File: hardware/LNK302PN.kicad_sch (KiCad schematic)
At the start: 7 parts, among them J101 AC, J102 PWM, J103 380OUT, J104 380_BP2876D, J105 LOAD, J107 3V3, J108 380_LNK302PN

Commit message: LNK302PN
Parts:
- removed J101: AC, TerminalBlock_Phoenix:TerminalBlock_Phoenix_MKDS-1,5-2-5.08_1x02_P5.08mm_Horizontal, symbol Connector:Screw_Terminal_01x02
- removed J102: PWM, TerminalBlock_Phoenix:TerminalBlock_Phoenix_MKDS-1-2-3.81_1x02_P3.81mm_Horizontal, symbol Connector:Screw_Terminal_01x02
- removed J103: 380OUT, TerminalBlock_Phoenix:TerminalBlock_Phoenix_MKDS-1,5-2-5.08_1x02_P5.08mm_Horizontal, symbol Connector:Screw_Terminal_01x02
- removed J104: 380_BP2876D, TerminalBlock_Phoenix:TerminalBlock_Phoenix_MKDS-1,5-2-5.08_1x02_P5.08mm_Horizontal, symbol Connector:Screw_Terminal_01x02
- removed J105: LOAD, TerminalBlock_Phoenix:TerminalBlock_Phoenix_MKDS-1,5-2-5.08_1x02_P5.08mm_Horizontal, symbol Connector:Screw_Terminal_01x02
- removed J107: 3V3, TerminalBlock_Phoenix:TerminalBlock_Phoenix_MKDS-1,5-2-5.08_1x02_P5.08mm_Horizontal, symbol Connector:Screw_Terminal_01x02
- removed J108: 380_LNK302PN, TerminalBlock_Phoenix:TerminalBlock_Phoenix_MKDS-1,5-2-5.08_1x02_P5.08mm_Horizontal, symbol Connector:Screw_Terminal_01x02
- added C401, C404, C405: 100nF, Capacitor_THT:C_Disc_D5.0mm_W2.5mm_P5.00mm, symbol Device:C
- added C402: 10uF 16V, Capacitor_THT:CP_Radial_D5.0mm_P2.50mm, symbol Device:C_Polarized
- added C403: 470uF 10V, Capacitor_THT:CP_Radial_D10.0mm_P5.00mm, symbol Device:C_Polarized
- added C406: 100uF 10V, Capacitor_THT:CP_Radial_D6.3mm_P2.50mm, symbol Device:C_Polarized
- added D401: ES1J, Diode_THT:D_DO-41_SOD81_P7.62mm_Horizontal, symbol Device:D
- added D402: US1M, Diode_THT:D_DO-41_SOD81_P7.62mm_Horizontal, symbol Device:D
- added L401: 2.2mH, Inductor_THT:L_Radial_D10.0mm_P5.00mm_Fastron_07M, symbol Device:L
- added R401: 2.2K, Resistor_THT:R_Axial_DIN0207_L6.3mm_D2.5mm_P7.62mm_Horizontal, symbol Device:R
- added R402: 4.7K, Resistor_THT:R_Axial_DIN0207_L6.3mm_D2.5mm_P7.62mm_Horizontal, symbol Device:R
- added U401: AMS1117-3.3, Package_TO_SOT_SMD:SOT-223-3_TabPin2, symbol Regulator_Linear:AMS1117-3.3
- added U402: LNK306P, Package_DIP:PowerIntegrations_PDIP-8B, symbol Regulator_Switching:LNK306P
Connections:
- new net: C402.1, D402.1 (K), R402.1
- new net: C401.1, C402.2, D401.1 (K), L401.1, R401.1, U402.1 (S), U402.2 (S), U402.7 (S), U402.8 (S)
- new net: C401.2, U402.3 (BP)
- new net: R401.2, R402.2, U402.4 (FB)
- new net 380V: U402.5 (D)
- new net 3V3: C405.2, C406.1, U401.2 (VO)
- new net 5V: C403.1, C404.2, D402.2 (A), L401.2, U401.3 (VI)
- new net GND: C403.2, C404.1, C405.1, C406.2, D401.2 (A), U401.1 (GND)
- no-connect marks 1 -> 0
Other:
- removed sheet ACInput
- removed sheet BP2876D
- removed sheet BP2956XS
- removed sheet LNK302PN

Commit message: Prototype
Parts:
- renumbered C404 to C401, C401 to C402, C406 to C403, C402 to C404, C403 to C406, U402 to U401, U401 to U402
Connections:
- net 380V renamed 325V
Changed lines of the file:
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@@
 		)
 	)
-	(hierarchical_label "380V"
+	(hierarchical_label "325V"
 		(shape input)
 		(at 76.2 81.28 180)
@@
 		(dnp no)
 		(fields_autoplaced yes)
-		(property "Reference" "C402"
+		(property "Reference" "C404"
 			(at 179.07 72.7709 0)
 			(effects
@@
 			(project "NosLed"
 				(path "/473a9690-2801-417b-8084-b7ef486d51ca/28bc7e25-99ca-436a-bb17-be814d11a6d1"
-					(reference "C402")
+					(reference "C404")
 					(unit 1)
 				)
@@
 		(dnp no)
 		(fields_autoplaced yes)
-		(property "Reference" "C403"
+		(property "Reference" "C406"
 			(at 218.44 88.0109 0)
 			(effects
@@
 			(project "NosLed"
 				(path "/473a9690-2801-417b-8084-b7ef486d51ca/28bc7e25-99ca-436a-bb17-be814d11a6d1"
-					(reference "C403")
+					(reference "C406")
 					(unit 1)
 				)
@@
 		(dnp no)
 		(fields_autoplaced yes)
-		(property "Reference" "U402"
+		(property "Reference" "U401"
 			(at 109.22 88.9 0)
 			(effects
@@
 			(project ""
 				(path "/473a9690-2801-417b-8084-b7ef486d51ca/28bc7e25-99ca-436a-bb17-be814d11a6d1"
-					(reference "U402")
+					(reference "U401")
 					(unit 1)
 				)
@@
 		(dnp no)
 		(fields_autoplaced yes)
-		(property "Reference" "C404"
+		(property "Reference" "C401"
 			(at 123.19 125.7299 0)
 			(effects
@@
 			(project "NosLed"
 				(path "/473a9690-2801-417b-8084-b7ef486d51ca/28bc7e25-99ca-436a-bb17-be814d11a6d1"
-					(reference "C404")
+					(reference "C401")
 					(unit 1)
 				)
@@
 		(dnp no)
 		(fields_autoplaced yes)
-		(property "Reference" "C401"
+		(property "Reference" "C402"
 			(at 130.81 73.6599 0)
 			(effects
@@
 			(project "NosLed"
 				(path "/473a9690-2801-417b-8084-b7ef486d51ca/28bc7e25-99ca-436a-bb17-be814d11a6d1"
-					(reference "C401")
+					(reference "C402")
 					(unit 1)
 				)
@@
 		(dnp no)
 		(fields_autoplaced yes)
-		(property "Reference" "C406"
+		(property "Reference" "C403"
 			(at 158.75 124.8409 0)
 			(effects
@@
 			(project "NosLed"
 				(path "/473a9690-2801-417b-8084-b7ef486d51ca/28bc7e25-99ca-436a-bb17-be814d11a6d1"
-					(reference "C406")
+					(reference "C403")
 					(unit 1)
 				)
@@
 		(dnp no)
 		(fields_autoplaced yes)
-		(property "Reference" "U401"
+		(property "Reference" "U402"
 			(at 143.51 111.76 0)
 			(effects
@@
 			(project ""
 				(path "/473a9690-2801-417b-8084-b7ef486d51ca/28bc7e25-99ca-436a-bb17-be814d11a6d1"
-					(reference "U401")
-					(unit 1)
-				)
+					(reference "U402")
+					(unit 1)
+				)

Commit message: Tracing draft
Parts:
- removed C401, C405: 100nF, Capacitor_THT:C_Disc_D5.0mm_W2.5mm_P5.00mm, symbol Device:C
- removed C403: 100uF 10V, Capacitor_THT:CP_Radial_D6.3mm_P2.50mm, symbol Device:C_Polarized
- removed C404: 10uF 16V, Capacitor_THT:CP_Radial_D5.0mm_P2.50mm, symbol Device:C_Polarized
- removed D401: ES1J, Diode_THT:D_DO-41_SOD81_P7.62mm_Horizontal, symbol Device:D
- removed D402: US1M, Diode_THT:D_DO-41_SOD81_P7.62mm_Horizontal, symbol Device:D
- removed U401: LNK306P, Package_DIP:PowerIntegrations_PDIP-8B, symbol Regulator_Switching:LNK306P
- removed U402: AMS1117-3.3, Package_TO_SOT_SMD:SOT-223-3_TabPin2, symbol Regulator_Linear:AMS1117-3.3
- added C402: 10uF 16V, Capacitor_SMD:C_0805_2012Metric_Pad1.18x1.45mm_HandSolder, symbol Device:C
- added D401, D402: US1M, Diode_SMD:D_SMA, symbol Diode:US1M
- added U401: LNK306D, Package_SO:SOIC-8_3.9x4.9mm_P1.27mm, symbol Regulator_Switching:LNK306D
- C401: renamed from C402; footprint Capacitor_THT:C_Disc_D5.0mm_W2.5mm_P5.00mm -> Capacitor_SMD:C_0201_0603Metric_Pad0.64x0.40mm_HandSolder
- L401: footprint Inductor_THT:L_Radial_D10.0mm_P5.00mm_Fastron_07M -> Inductor_THT:L_Radial_D12.0mm_P5.00mm_Neosid_SD12k_style2
- R401, R402: footprint Resistor_THT:R_Axial_DIN0207_L6.3mm_D2.5mm_P7.62mm_Horizontal -> Resistor_SMD:R_0201_0603Metric_Pad0.64x0.40mm_HandSolder
- renumbered C406 to C403
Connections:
- net 325V: now also U401.4 (D)
- net 5V: now also D402.1 (K)
- net GND: now also D401.2 (A)
- net at R402.1: now also C402.2, D402.2 (A)
- net at C401.1, L401.1, R401.1: now also C402.1, D401.1 (K), U401.5 (S), U401.6 (S), U401.7 (S), U401.8 (S)
- net at C401.2: now also U401.1 (BP)
- net at R401.2, R402.2: now also U401.2 (FB)

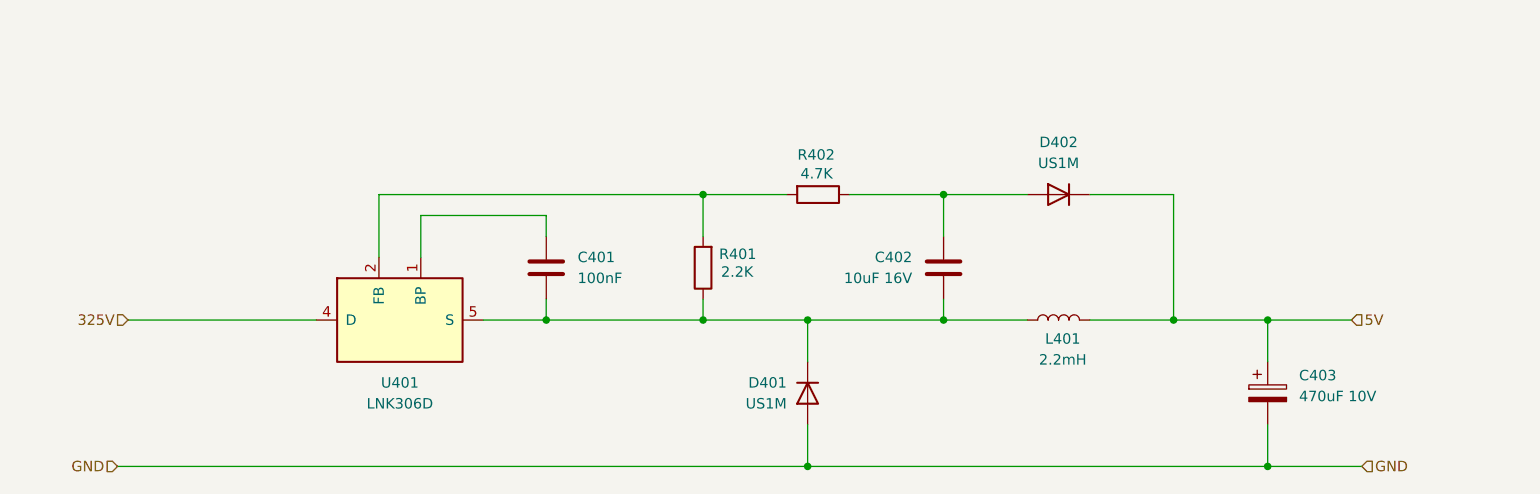
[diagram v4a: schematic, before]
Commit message: Tracing 0.2
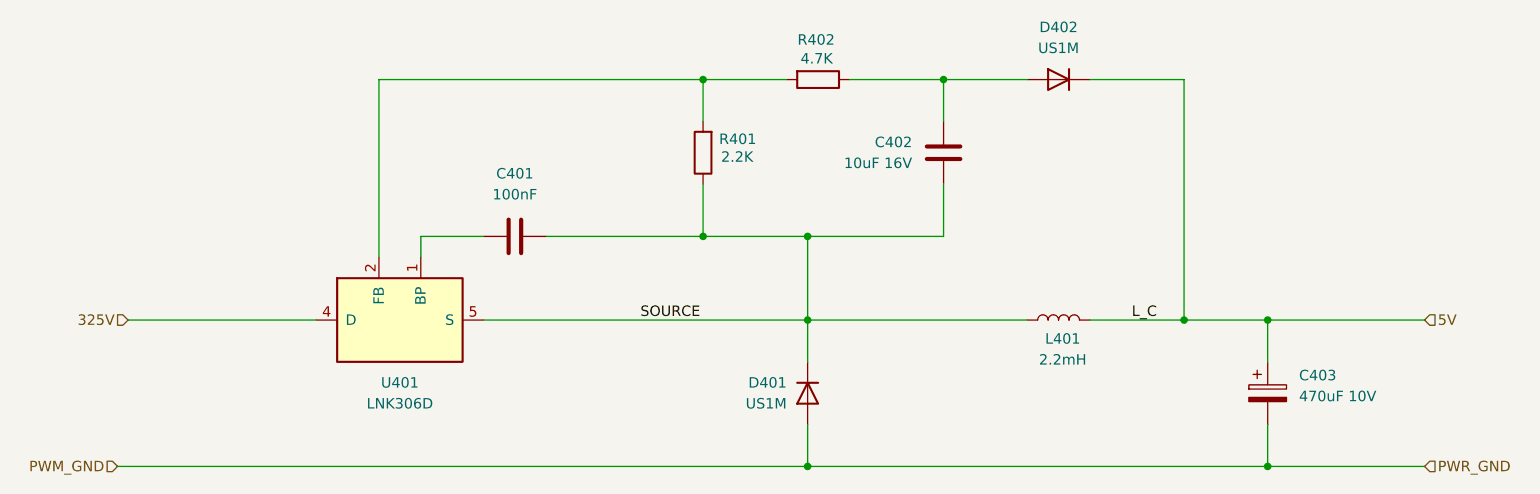
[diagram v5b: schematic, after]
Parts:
- C401: footprint Capacitor_SMD:C_0201_0603Metric_Pad0.64x0.40mm_HandSolder -> Capacitor_SMD:C_0603_1608Metric_Pad1.08x0.95mm_HandSolder
- C403: footprint Capacitor_THT:CP_Radial_D10.0mm_P5.00mm -> Capacitor_THT:CP_Radial_D8.0mm_P5.00mm
- L401: footprint Inductor_THT:L_Radial_D12.0mm_P5.00mm_Neosid_SD12k_style2 -> Inductor_THT:L_Radial_D9.5mm_P5.00mm_Fastron_07HVP
- R401, R402: footprint Resistor_SMD:R_0201_0603Metric_Pad0.64x0.40mm_HandSolder -> Resistor_SMD:R_0603_1608Metric_Pad0.98x0.95mm_HandSolder
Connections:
- net SOURCE: now reaches C401.1, C402.1, D401.1 (K), L401.1, R401.1, U401.5 (S), U401.6 (S), U401.7 (S), U401.8 (S)
- net GND renamed PWM_GND
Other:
- moved on the sheet: C401, C402, D402, R401, R402

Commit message: Version 1
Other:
- moved on the sheet: D401
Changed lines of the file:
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@@
-	)
-	(junction
-		(at 158.75 99.06)
-		(diameter 0)
-		(color 0 0 0 0)
 	)
 	(junction
@@
 	)
 	(junction
+		(at 175.26 71.12)
+		(diameter 0)
+		(color 0 0 0 0)
+	)
+	(junction
 		(at 146.05 71.12)
 		(diameter 0)
@@
 	)
 	(junction
-		(at 158.75 81.28)
+		(at 175.26 81.28)
 		(diameter 0)
 		(color 0 0 0 0)
 	)
 	(junction
-		(at 158.75 71.12)
+		(at 175.26 99.06)
 		(diameter 0)
 		(color 0 0 0 0)
@@
 	(wire
 		(pts
-			(xy 158.75 99.06) (xy 214.63 99.06)
-		)
-		(stroke
-			(width 0)
-			(type default)
-		)
-	)
-	(wire
-		(pts
-			(xy 158.75 81.28) (xy 185.42 81.28)
-		)
-		(stroke
-			(width 0)
-			(type default)
-		)
-	)
-	(wire
-		(pts
 			(xy 204.47 52.07) (xy 204.47 81.28)
 		)
@@
 	(wire
 		(pts
-			(xy 158.75 71.12) (xy 158.75 81.28)
+			(xy 175.26 81.28) (xy 185.42 81.28)
+		)
+		(stroke
+			(width 0)
+			(type default)
+		)
+	)
+	(wire
+		(pts
+			(xy 175.26 71.12) (xy 175.26 81.28)
 		)
 		(stroke
@@
 	(wire
 		(pts
-			(xy 158.75 86.36) (xy 158.75 81.28)
+			(xy 175.26 86.36) (xy 175.26 81.28)
 		)
 		(stroke
@@
 	(wire
 		(pts
-			(xy 119.38 81.28) (xy 158.75 81.28)
-		)
-		(stroke
-			(width 0)
-			(type default)
-		)
-	)
-	(wire
-		(pts
-			(xy 158.75 71.12) (xy 175.26 71.12)
-		)
-		(stroke
-			(width 0)
-			(type default)
-		)
-	)
-	(wire
-		(pts
-			(xy 74.93 99.06) (xy 158.75 99.06)
+			(xy 119.38 81.28) (xy 175.26 81.28)
+		)
+		(stroke
+			(width 0)
+			(type default)
+		)
+	)
+	(wire
+		(pts
+			(xy 74.93 99.06) (xy 175.26 99.06)
 		)
 		(stroke
@@
 	(wire
 		(pts
-			(xy 158.75 93.98) (xy 158.75 99.06)
+			(xy 175.26 93.98) (xy 175.26 99.06)
 		)
 		(stroke
@@
 	(wire
 		(pts
-			(xy 146.05 71.12) (xy 158.75 71.12)
+			(xy 146.05 71.12) (xy 175.26 71.12)
+		)
+		(stroke
+			(width 0)
+			(type default)
+		)
+	)
+	(wire
+		(pts
+			(xy 175.26 99.06) (xy 214.63 99.06)
 		)
 		(stroke
@@
 	(symbol
 		(lib_id "Diode:US1M")
-		(at 158.75 90.17 90)
+		(at 175.26 90.17 90)
 		(mirror x)
 		(unit 1)
@@
 		(dnp no)
 		(property "Reference" "D401"
-			(at 156.21 88.8999 90)
+			(at 172.72 88.8999 90)
 			(effects
 				(font
@@
 		)
 		(property "Value" "US1M"
-			(at 156.21 91.4399 90)
+			(at 172.72 91.4399 90)
 			(effects
 				(font
@@
 		)
 		(property "Footprint" "Diode_SMD:D_SMA"
-			(at 163.195 90.17 0)
+			(at 179.705 90.17 0)
 			(effects
 				(font
@@
 		)
 		(property "Datasheet" "https://www.diodes.com/assets/Datasheets/ds16008.pdf"
-			(at 158.75 90.17 0)
+			(at 175.26 90.17 0)
 			(effects
 				(font
@@
 		)
 		(property "Description" "1000V, 1A, General Purpose Rectifier Diode, SMA(DO-214AC)"
-			(at 158.75 90.17 0)
+			(at 175.26 90.17 0)
 			(effects
 				(font
@@
 		)
 		(property "Sim.Device" "D"
-			(at 158.75 90.17 0)
+			(at 175.26 90.17 0)
 			(effects
 				(font
@@
 		)
 		(property "Sim.Pins" "1=K 2=A"
-			(at 158.75 90.17 0)
-			(effects
-				(font
+			(at 175.26 90.17 0)
+			(effects
+				(font

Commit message: Fixes
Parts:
- renumbered C402 to C401, C401 to C402, D402 to D401, D401 to D402, R402 to R401, R401 to R402
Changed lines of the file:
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@@
-	)
-	(junction
-		(at 214.63 99.06)
-		(diameter 0)
-		(color 0 0 0 0)
 	)
 	(junction
@@
 	)
 	(junction
+		(at 130.81 81.28)
+		(diameter 0)
+		(color 0 0 0 0)
+	)
+	(junction
 		(at 175.26 99.06)
 		(diameter 0)
@@
 	(wire
 		(pts
-			(xy 214.63 99.06) (xy 233.68 99.06)
-		)
-		(stroke
-			(width 0)
-			(type default)
-		)
-	)
-	(wire
-		(pts
-			(xy 119.38 81.28) (xy 175.26 81.28)
+			(xy 119.38 81.28) (xy 130.81 81.28)
 		)
 		(stroke
@@
 		(pts
 			(xy 146.05 52.07) (xy 106.68 52.07)
+		)
+		(stroke
+			(width 0)
+			(type default)
+		)
+	)
+	(wire
+		(pts
+			(xy 130.81 81.28) (xy 175.26 81.28)
 		)
 		(stroke
@@
 		)
 	)
-	(label "L_C"
-		(at 198.12 81.28 0)
-		(effects
-			(font
-				(size 1.27 1.27)
-			)
-			(justify left bottom)
-		)
-	)
 	(hierarchical_label "5V"
 		(shape input)
 		(at 233.68 81.28 0)
-		(effects
-			(font
-				(size 1.27 1.27)
-			)
-			(justify left)
-		)
-	)
-	(hierarchical_label "PWR_GND"
-		(shape input)
-		(at 233.68 99.06 0)
 		(effects
 			(font
@@
 		(on_board yes)
 		(dnp no)
-		(property "Reference" "R402"
+		(property "Reference" "R401"
 			(at 162.052 47.244 90)
 			(effects
@@
 			(project "NosLed"
 				(path "/473a9690-2801-417b-8084-b7ef486d51ca/28bc7e25-99ca-436a-bb17-be814d11a6d1"
-					(reference "R402")
+					(reference "R401")
 					(unit 1)
 				)
@@
 		(dnp no)
 		(fields_autoplaced yes)
-		(property "Reference" "C401"
+		(property "Reference" "C402"
 			(at 123.19 63.5 90)
 			(effects
@@
 			(project "NosLed"
 				(path "/473a9690-2801-417b-8084-b7ef486d51ca/28bc7e25-99ca-436a-bb17-be814d11a6d1"
-					(reference "C401")
+					(reference "C402")
 					(unit 1)
 				)
@@
 		(on_board yes)
 		(dnp no)
-		(property "Reference" "R401"
+		(property "Reference" "R402"
 			(at 152.527 59.309 0)
 			(effects
@@
 			(project "NosLed"
 				(path "/473a9690-2801-417b-8084-b7ef486d51ca/28bc7e25-99ca-436a-bb17-be814d11a6d1"
-					(reference "R401")
+					(reference "R402")
+					(unit 1)
+				)
+			)
+		)
+	)
+	(symbol
+		(lib_id "power:PWR_FLAG")
+		(at 130.81 81.28 0)
+		(unit 1)
+		(exclude_from_sim no)
+		(in_bom yes)
+		(on_board yes)
+		(dnp no)
+		(fields_autoplaced yes)
+		(property "Reference" "#FLG0401"
+			(at 130.81 79.375 0)
+			(effects
+				(font
+					(size 1.27 1.27)
+				)
+				(hide yes)
+			)
+		)
+		(property "Value" "PWR_FLAG"
+			(at 130.81 76.2 0)
+			(effects
+				(font
+					(size 1.27 1.27)
+				)
+			)
+		)
+		(property "Footprint" ""
+			(at 130.81 81.28 0)
+			(effects
+				(font
+					(size 1.27 1.27)
+				)
+				(hide yes)
+			)
+		)
+		(property "Datasheet" "~"
+			(at 130.81 81.28 0)
+			(effects
+				(font
+					(size 1.27 1.27)
+				)
+				(hide yes)
+			)
+		)
+		(property "Description" "Special symbol for telling ERC where power comes from"
+			(at 130.81 81.28 0)
+			(effects
+				(font
+					(size 1.27 1.27)
+				)
+				(hide yes)
+			)
+		)
+		(pin "1"
+		)
+		(instances
+			(project ""
+				(path "/473a9690-2801-417b-8084-b7ef486d51ca/28bc7e25-99ca-436a-bb17-be814d11a6d1"
+					(reference "#FLG0401")
 					(unit 1)
 				)
@@
 		(on_board yes)
 		(dnp no)
-		(property "Reference" "C402"
+		(property "Reference" "C401"
 			(at 171.45 59.6899 0)
 			(effects
@@
 			(project "NosLed"
 				(path "/473a9690-2801-417b-8084-b7ef486d51ca/28bc7e25-99ca-436a-bb17-be814d11a6d1"
-					(reference "C402")
+					(reference "C401")
 					(unit 1)
 				)
@@
 		(on_board yes)
 		(dnp no)
-		(property "Reference" "D402"
+		(property "Reference" "D401"
 			(at 189.23 45.72 0)
 			(effects
@@
 			(project "NosLed"
 				(path "/473a9690-2801-417b-8084-b7ef486d51ca/28bc7e25-99ca-436a-bb17-be814d11a6d1"
-					(reference "D402")
+					(reference "D401")
 					(unit 1)
 				)
@@
 		(on_board yes)
 		(dnp no)
-		(property "Reference" "D401"
+		(property "Reference" "D402"
 			(at 172.72 88.8999 90)
 			(effects
@@
 			(project "NosLed"
 				(path "/473a9690-2801-417b-8084-b7ef486d51ca/28bc7e25-99ca-436a-bb17-be814d11a6d1"
-					(reference "D401")
-					(unit 1)
-				)
+					(reference "D402")
+					(unit 1)
+				)

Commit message: Use non-hand soldering footprints
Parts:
- C401: footprint Capacitor_SMD:C_0805_2012Metric_Pad1.18x1.45mm_HandSolder -> Capacitor_SMD:C_0805_2012Metric
- C402: footprint Capacitor_SMD:C_0603_1608Metric_Pad1.08x0.95mm_HandSolder -> Capacitor_SMD:C_0603_1608Metric
- R401, R402: footprint Resistor_SMD:R_0603_1608Metric_Pad0.98x0.95mm_HandSolder -> Resistor_SMD:R_0603_1608Metric
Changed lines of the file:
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@@
 			)
 		)
-		(property "Footprint" "Resistor_SMD:R_0603_1608Metric_Pad0.98x0.95mm_HandSolder"
+		(property "Footprint" "Resistor_SMD:R_0603_1608Metric"
 			(at 160.02 50.292 90)
 			(effects
@@
 			)
 		)
-		(property "Footprint" "Capacitor_SMD:C_0603_1608Metric_Pad1.08x0.95mm_HandSolder"
+		(property "Footprint" "Capacitor_SMD:C_0603_1608Metric"
 			(at 119.38 72.0852 0)
 			(effects
@@
 			)
 		)
-		(property "Footprint" "Resistor_SMD:R_0603_1608Metric_Pad0.98x0.95mm_HandSolder"
+		(property "Footprint" "Resistor_SMD:R_0603_1608Metric"
 			(at 147.828 60.96 90)
 			(effects
@@
 			)
 		)
-		(property "Footprint" "Capacitor_SMD:C_0805_2012Metric_Pad1.18x1.45mm_HandSolder"
+		(property "Footprint" "Capacitor_SMD:C_0805_2012Metric"
 			(at 176.2252 57.15 0)
 			(effects
